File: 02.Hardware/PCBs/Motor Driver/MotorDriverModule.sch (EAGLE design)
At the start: 45 parts, among them Q1 DMC3021LSD-13, Q2 DMC3021LSD-13, Q3 DMC3021LSD-13, U1 FAN3268TMX, U2 FAN3268TMX, U3 FAN3268TMX, U4 MCP6001T-I_LT

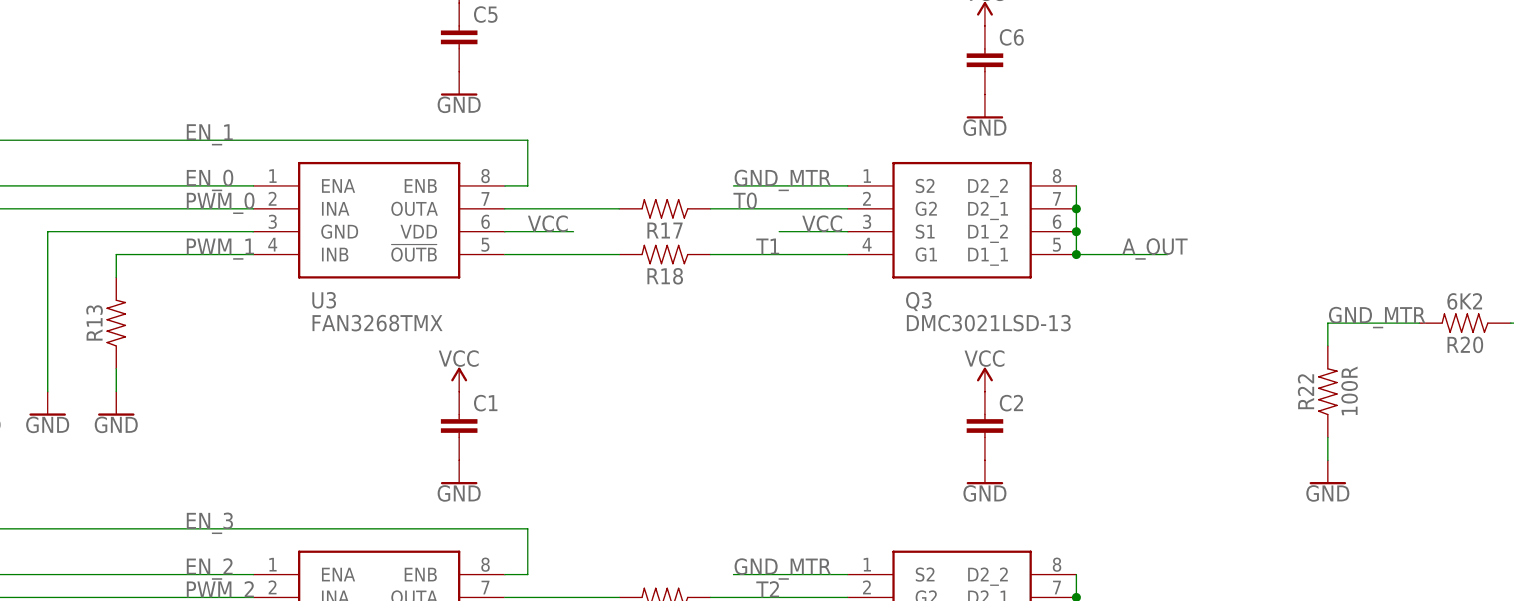
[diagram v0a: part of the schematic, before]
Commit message: Cambios de rutado y nombres
Cambios de rutado y nombres
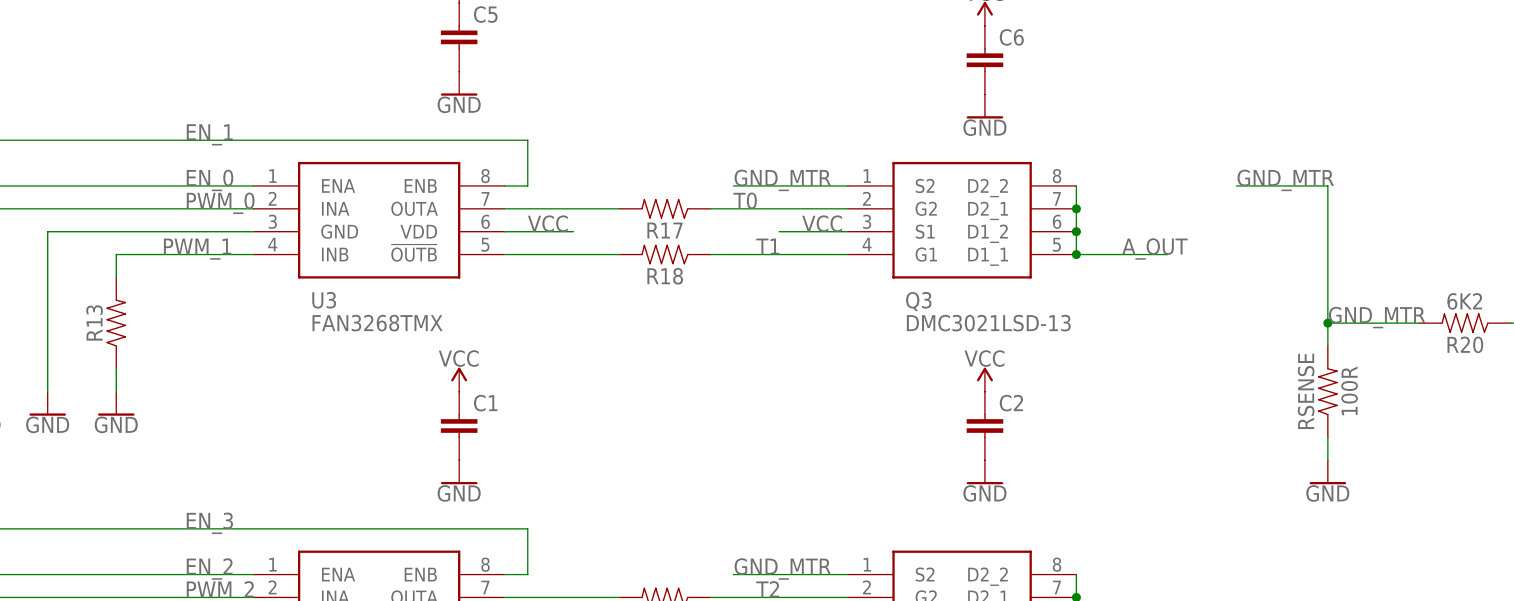
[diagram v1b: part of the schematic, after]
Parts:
- renumbered R22 to RSENSE
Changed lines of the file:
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@@
 <part name="R20" library="SparkFun-Resistors" library_urn="urn:adsk.eagle:library:532" deviceset="RESISTOR" device="0805" package3d_urn="urn:adsk.eagle:package:39651/1" value="6K2"/>
 <part name="R21" library="SparkFun-Resistors" library_urn="urn:adsk.eagle:library:532" deviceset="RESISTOR" device="0805" package3d_urn="urn:adsk.eagle:package:39651/1" value="9K1"/>
-<part name="R22" library="SparkFun-Resistors" library_urn="urn:adsk.eagle:library:532" deviceset="RESISTOR" device="1206" package3d_urn="urn:adsk.eagle:package:39654/1" value="100R"/>
+<part name="RSENSE" library="SparkFun-Resistors" library_urn="urn:adsk.eagle:library:532" deviceset="RESISTOR" device="1206" package3d_urn="urn:adsk.eagle:package:39654/1" value="100R"/>
 <part name="GND22" library="SparkFun-PowerSymbols" library_urn="urn:adsk.eagle:library:530" deviceset="GND" device=""/>
 <part name="GND23" library="SparkFun-PowerSymbols" library_urn="urn:adsk.eagle:library:530" deviceset="GND" device=""/>
@@
 <attribute name="VALUE" x="238.76" y="133.604" size="1.778" layer="96" font="vector" rot="R180" align="top-center"/>
 </instance>
-<instance part="R22" gate="G$1" x="175.26" y="101.6" smashed="yes" rot="R90">
+<instance part="RSENSE" gate="G$1" x="175.26" y="101.6" smashed="yes" rot="R90">
 <attribute name="NAME" x="173.736" y="101.6" size="1.778" layer="95" font="vector" rot="R90" align="bottom-center"/>
 <attribute name="VALUE" x="176.784" y="101.6" size="1.778" layer="96" font="vector" rot="R90" align="top-center"/>
@@
 <segment>
 <pinref part="GND22" gate="1" pin="GND"/>
-<pinref part="R22" gate="G$1" pin="1"/>
+<pinref part="RSENSE" gate="G$1" pin="1"/>
 <wire x1="175.26" y1="96.52" x2="175.26" y2="93.98" width="0.1524" layer="91"/>
 </segment>
@@
 </segment>
 <segment>
-<pinref part="R22" gate="G$1" pin="2"/>
+<pinref part="RSENSE" gate="G$1" pin="2"/>
 <pinref part="R20" gate="G$1" pin="2"/>
 <wire x1="175.26" y1="106.68" x2="175.26" y2="109.22" width="0.1524" layer="91"/>
 <wire x1="175.26" y1="109.22" x2="185.42" y2="109.22" width="0.1524" layer="91"/>
 <label x="175.26" y="109.22" size="1.778" layer="95"/>
+<wire x1="175.26" y1="109.22" x2="175.26" y2="124.46" width="0.1524" layer="91"/>
+<junction x="175.26" y="109.22"/>
+<wire x1="175.26" y1="124.46" x2="165.1" y2="124.46" width="0.1524" layer="91"/>
+<label x="165.1" y="124.46" size="1.778" layer="95"/>
 </segment>
 </net>
@@
 <wire x1="40.64" y1="114.3" x2="40.64" y2="116.84" width="0.1524" layer="91"/>
 <wire x1="40.64" y1="116.84" x2="55.88" y2="116.84" width="0.1524" layer="91"/>
-<label x="48.26" y="116.84" size="1.778" layer="95"/>
-</segment>
-<segment>
+<label x="45.72" y="116.84" size="1.778" layer="95"/>
+</segment>
+<segment>

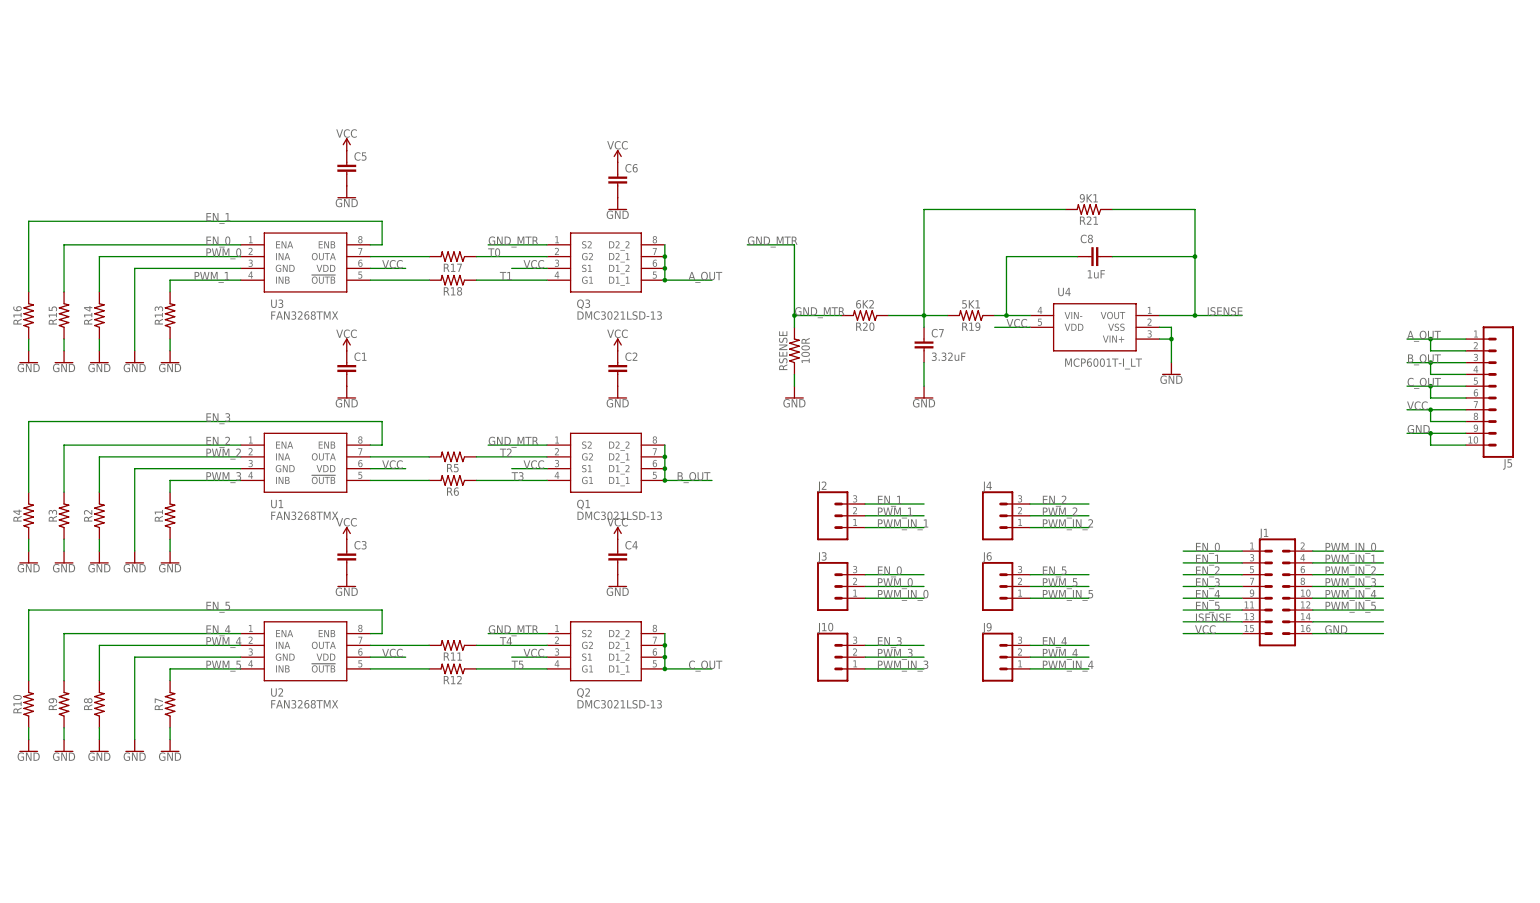
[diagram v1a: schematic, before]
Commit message: v2 Cambio de conector de entrada y correccion de errores
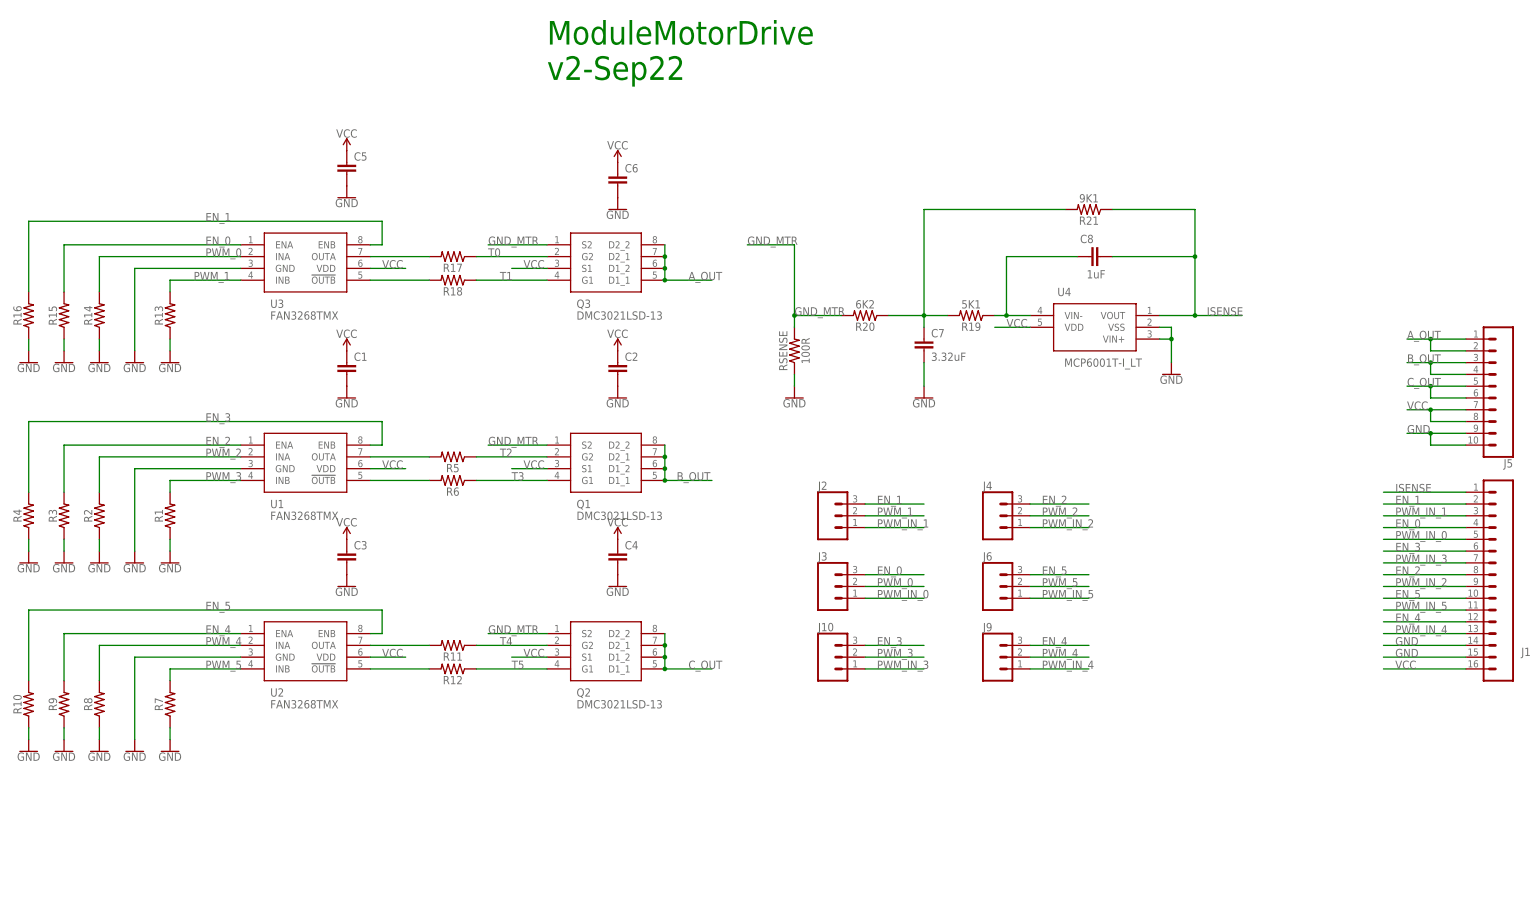
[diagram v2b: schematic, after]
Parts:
- J1: device SparkFun-Connectors:CONN_08X2 -> SparkFun-Connectors:CONN_16
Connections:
- removed net N$27: J1.14
- net EN_0: now also J1.4; no longer J1.1
- net EN_1: now also J1.2; no longer J1.3
- net EN_2: now also J1.8; no longer J1.5
- net EN_3: now also J1.6; no longer J1.7
- net EN_4: now also J1.12; no longer J1.9
- net EN_5: now also J1.10; no longer J1.11
- net GND: now also J1.14, J1.15; no longer J1.16
- net ISENSE: now also J1.1; no longer J1.13
- net PWM_IN_0: now also J1.5; no longer J1.2
- net PWM_IN_1: now also J1.3; no longer J1.4
- net PWM_IN_2: now also J1.9; no longer J1.6
- net PWM_IN_3: now also J1.7; no longer J1.8
- net PWM_IN_4: now also J1.13; no longer J1.10
- net PWM_IN_5: now also J1.11; no longer J1.12
- net VCC: now also J1.16; no longer J1.15
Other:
- note added: "ModuleMotorDrive v2-Sep22"
- moved on the sheet: J1
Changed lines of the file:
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@@
 <part name="SUPPLY5" library="SparkFun-PowerSymbols" library_urn="urn:adsk.eagle:library:530" deviceset="VCC" device=""/>
 <part name="SUPPLY6" library="SparkFun-PowerSymbols" library_urn="urn:adsk.eagle:library:530" deviceset="VCC" device=""/>
-<part name="J1" library="SparkFun-Connectors" library_urn="urn:adsk.eagle:library:513" deviceset="CONN_08X2" device="" package3d_urn="urn:adsk.eagle:package:38152/1"/>
+<part name="J1" library="SparkFun-Connectors" library_urn="urn:adsk.eagle:library:513" deviceset="CONN_16" device="" package3d_urn="urn:adsk.eagle:package:38258/1"/>
 <part name="J2" library="SparkFun-Connectors" library_urn="urn:adsk.eagle:library:513" deviceset="CONN_03" device="" package3d_urn="urn:adsk.eagle:package:38063/1"/>
 <part name="J3" library="SparkFun-Connectors" library_urn="urn:adsk.eagle:library:513" deviceset="CONN_03" device="" package3d_urn="urn:adsk.eagle:package:38063/1"/>
@@
 <sheet>
 <plain>
+<text x="121.92" y="160.02" size="5.08" layer="91">ModuleMotorDrive
+v2-Sep22</text>
 </plain>
 <instances>
@@
 <attribute name="VALUE" x="137.16" y="145.034" size="1.778" layer="96" align="bottom-center"/>
 </instance>
-<instance part="J1" gate="G$1" x="279.4" y="48.26" smashed="yes">
-<attribute name="VALUE" x="275.59" y="35.814" size="1.778" layer="96" font="vector"/>
-<attribute name="NAME" x="275.59" y="61.468" size="1.778" layer="95" font="vector"/>
+<instance part="J1" gate="G$1" x="330.2" y="50.8" smashed="yes" rot="R180">
+<attribute name="VALUE" x="334.01" y="63.246" size="1.778" layer="96" font="vector" rot="R180"/>
+<attribute name="NAME" x="334.01" y="37.592" size="1.778" layer="95" font="vector" rot="R180"/>
 </instance>
 <instance part="J2" gate="J$1" x="182.88" y="66.04" smashed="yes">
@@
 <pinref part="R16" gate="G$1" pin="1"/>
 <wire x1="10.16" y1="101.6" x2="10.16" y2="104.14" width="0.1524" layer="91"/>
-</segment>
-<segment>
-<pinref part="J1" gate="G$1" pin="16"/>
-<wire x1="287.02" y1="40.64" x2="302.26" y2="40.64" width="0.1524" layer="91"/>
-<label x="289.56" y="40.64" size="1.778" layer="95"/>
 </segment>
 <segment>
@@
 <label x="307.34" y="83.82" size="1.778" layer="95"/>
 </segment>
+<segment>
+<pinref part="J1" gate="G$1" pin="14"/>
+<wire x1="320.04" y1="38.1" x2="302.26" y2="38.1" width="0.1524" layer="91"/>
+<label x="304.8" y="38.1" size="1.778" layer="95"/>
+</segment>
+<segment>
+<pinref part="J1" gate="G$1" pin="15"/>
+<wire x1="320.04" y1="35.56" x2="302.26" y2="35.56" width="0.1524" layer="91"/>
+<label x="304.8" y="35.56" size="1.778" layer="95"/>
+</segment>
 </net>
 <net name="PWM_3" class="0">
@@
 </segment>
 <segment>
-<pinref part="J1" gate="G$1" pin="7"/>
-<wire x1="271.78" y1="50.8" x2="259.08" y2="50.8" width="0.1524" layer="91"/>
-<label x="261.62" y="50.8" size="1.778" layer="95"/>
+<pinref part="J1" gate="G$1" pin="6"/>
+<wire x1="320.04" y1="58.42" x2="302.26" y2="58.42" width="0.1524" layer="91"/>
+<label x="304.8" y="58.42" size="1.778" layer="95"/>
 </segment>
 </net>
@@
 </segment>
 <segment>
-<pinref part="J1" gate="G$1" pin="15"/>
-<wire x1="271.78" y1="40.64" x2="259.08" y2="40.64" width="0.1524" layer="91"/>
-<label x="261.62" y="40.64" size="1.778" layer="95"/>
-</segment>
-<segment>
 <pinref part="U4" gate="G$1" pin="VDD"/>
 <wire x1="226.06" y1="106.68" x2="218.44" y2="106.68" width="0.1524" layer="91"/>
@@
 <junction x="312.42" y="88.9"/>
 <label x="307.34" y="88.9" size="1.778" layer="95"/>
+</segment>
+<segment>
+<pinref part="J1" gate="G$1" pin="16"/>
+<wire x1="320.04" y1="33.02" x2="302.26" y2="33.02" width="0.1524" layer="91"/>
+<label x="304.8" y="33.02" size="1.778" layer="95"/>
 </segment>
 </net>
@@
 </segment>
 <segment>
-<pinref part="J1" gate="G$1" pin="9"/>
-<wire x1="271.78" y1="48.26" x2="259.08" y2="48.26" width="0.1524" layer="91"/>
-<label x="261.62" y="48.26" size="1.778" layer="95"/>
+<pinref part="J1" gate="G$1" pin="12"/>
+<wire x1="320.04" y1="43.18" x2="302.26" y2="43.18" width="0.1524" layer="91"/>
+<label x="304.8" y="43.18" size="1.778" layer="95"/>
 </segment>
 </net>
@@
 </segment>
 <segment>
-<pinref part="J1" gate="G$1" pin="11"/>
-<wire x1="271.78" y1="45.72" x2="259.08" y2="45.72" width="0.1524" layer="91"/>
-<label x="261.62" y="45.72" size="1.778" layer="95"/>
+<pinref part="J1" gate="G$1" pin="10"/>
+<wire x1="320.04" y1="48.26" x2="302.26" y2="48.26" width="0.1524" layer="91"/>
+<label x="304.8" y="48.26" size="1.778" layer="95"/>
 </segment>
 </net>
@@
 </segment>
 <segment>
-<pinref part="J1" gate="G$1" pin="1"/>
-<wire x1="271.78" y1="58.42" x2="259.08" y2="58.42" width="0.1524" layer="91"/>
-<label x="261.62" y="58.42" size="1.778" layer="95"/>
+<pinref part="J1" gate="G$1" pin="4"/>
+<wire x1="320.04" y1="63.5" x2="302.26" y2="63.5" width="0.1524" layer="91"/>
+<label x="304.8" y="63.5" size="1.778" layer="95"/>
 </segment>
 </net>
@@
 </segment>
 <segment>
-<pinref part="J1" gate="G$1" pin="3"/>
-<wire x1="271.78" y1="55.88" x2="259.08" y2="55.88" width="0.1524" layer="91"/>
-<label x="261.62" y="55.88" size="1.778" layer="95"/>
+<pinref part="J1" gate="G$1" pin="2"/>
+<wire x1="320.04" y1="68.58" x2="302.26" y2="68.58" width="0.1524" layer="91"/>
+<label x="304.8" y="68.58" size="1.778" layer="95"/>
 </segment>
 </net>
@@
 </segment>
 <segment>
-<pinref part="J1" gate="G$1" pin="5"/>
-<wire x1="271.78" y1="53.34" x2="259.08" y2="53.34" width="0.1524" layer="91"/>
-<label x="261.62" y="53.34" size="1.778" layer="95"/>
+<pinref part="J1" gate="G$1" pin="8"/>
+<wire x1="320.04" y1="53.34" x2="302.26" y2="53.34" width="0.1524" layer="91"/>
+<label x="304.8" y="53.34" size="1.778" layer="95"/>
 </segment>
 </net>
@@
 </segment>
 <segment>
-<pinref part="J1" gate="G$1" pin="4"/>
-<wire x1="287.02" y1="55.88" x2="302.26" y2="55.88" width="0.1524" layer="91"/>
-<label x="289.56" y="55.88" size="1.778" layer="95"/>
+<pinref part="J1" gate="G$1" pin="3"/>
+<wire x1="320.04" y1="66.04" x2="302.26" y2="66.04" width="0.1524" layer="91"/>
+<label x="304.8" y="66.04" size="1.778" layer="95"/>
 </segment>
 </net>
@@
 </segment>
 <segment>
-<pinref part="J1" gate="G$1" pin="2"/>
-<wire x1="287.02" y1="58.42" x2="302.26" y2="58.42" width="0.1524" layer="91"/>
-<label x="289.56" y="58.42" size="1.778" layer="95"/>
+<pinref part="J1" gate="G$1" pin="5"/>
+<wire x1="320.04" y1="60.96" x2="302.26" y2="60.96" width="0.1524" layer="91"/>
+<label x="304.8" y="60.96" size="1.778" layer="95"/>
 </segment>
 </net>
@@
 </segment>
 <segment>
-<pinref part="J1" gate="G$1" pin="8"/>
-<wire x1="287.02" y1="50.8" x2="302.26" y2="50.8" width="0.1524" layer="91"/>
-<label x="289.56" y="50.8" size="1.778" layer="95"/>
+<pinref part="J1" gate="G$1" pin="7"/>
+<wire x1="320.04" y1="55.88" x2="302.26" y2="55.88" width="0.1524" layer="91"/>
+<label x="304.8" y="55.88" size="1.778" layer="95"/>
 </segment>
 </net>
@@
 </segment>
 <segment>
-<pinref part="J1" gate="G$1" pin="6"/>
-<wire x1="287.02" y1="53.34" x2="302.26" y2="53.34" width="0.1524" layer="91"/>
-<label x="289.56" y="53.34" size="1.778" layer="95"/>
+<pinref part="J1" gate="G$1" pin="9"/>
+<wire x1="320.04" y1="50.8" x2="302.26" y2="50.8" width="0.1524" layer="91"/>
+<label x="304.8" y="50.8" size="1.778" layer="95"/>
 </segment>
 </net>
@@
 </segment>
 <segment>
-<pinref part="J1" gate="G$1" pin="12"/>
-<wire x1="287.02" y1="45.72" x2="302.26" y2="45.72" width="0.1524" layer="91"/>
-<label x="289.56" y="45.72" size="1.778" layer="95"/>
+<pinref part="J1" gate="G$1" pin="11"/>
+<wire x1="320.04" y1="45.72" x2="302.26" y2="45.72" width="0.1524" layer="91"/>
+<label x="304.8" y="45.72" size="1.778" layer="95"/>
 </segment>
 </net>
@@
 </segment>
 <segment>
-<pinref part="J1" gate="G$1" pin="10"/>
-<wire x1="287.02" y1="48.26" x2="302.26" y2="48.26" width="0.1524" layer="91"/>
-<label x="289.56" y="48.26" size="1.778" layer="95"/>
-</segment>
-</net>
-<net name="N$27" class="0">
-<segment>
-<pinref part="J1" gate="G$1" pin="14"/>
-<wire x1="287.02" y1="43.18" x2="302.26" y2="43.18" width="0.1524" layer="91"/>
+<pinref part="J1" gate="G$1" pin="13"/>
+<wire x1="320.04" y1="40.64" x2="302.26" y2="40.64" width="0.1524" layer="91"/>
+<label x="304.8" y="40.64" size="1.778" layer="95"/>
 </segment>
 </net>
@@
 </segment>
 <segment>
-<pinref part="J1" gate="G$1" pin="13"/>
-<wire x1="271.78" y1="43.18" x2="259.08" y2="43.18" width="0.1524" layer="91"/>
-<label x="261.62" y="43.18" size="1.778" layer="95"/>
+<pinref part="J1" gate="G$1" pin="1"/>
+<wire x1="320.04" y1="71.12" x2="302.26" y2="71.12" width="0.1524" layer="91"/>
+<label x="304.8" y="71.12" size="1.778" layer="95"/>
 </segment>
 </net>
@@
 </drawing>
 <compatibility>
+<note version="6.3" minversion="6.2.2" severity="warning">
+Since Version 6.2.2 text objects can contain more than one line,
+which will not be processed correctly with this version.
+</note>
 <note version="8.2" severity="warning">
 Since Version 8.2, EAGLE supports online libraries. The ids
